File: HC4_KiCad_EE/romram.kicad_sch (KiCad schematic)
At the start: 9 parts, among them J4 AVR-UPDI-6, U1 ATmega4809-A, U2 CH340E

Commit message: 配線進捗、7474を使った変な回路
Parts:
- removed CP11, CP12, CP13: 0.1u, Capacitor_SMD:C_0603_1608Metric, symbol Device2:C_Bypass
- added C2, C3, C4: 0.1u, Capacitor_SMD:C_0603_1608Metric, symbol Device:C
- renumbered C2 to C5
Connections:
- net GND: now also C2.2, C3.2, C4.2
- net VCC: now also C2.1, C3.1, C4.1
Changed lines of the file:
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@@
 		(on_board yes)
 		(dnp no)
-		(property "Reference" "C2"
+		(property "Reference" "C5"
 			(at 163.83 64.7699 0)
 			(effects
@@
 			(project ""
 				(path "/33731ded-38c0-4297-bdd8-92b082f46ff8/ee79785c-5138-4152-a60d-370cd803a828"
-					(reference "C2")
+					(reference "C5")
+					(unit 1)
+				)
+			)
+		)
+	)
+	(symbol
+		(lib_id "Device:C")
+		(at 132.08 163.83 0)
+		(mirror y)
+		(unit 1)
+		(exclude_from_sim no)
+		(in_bom yes)
+		(on_board yes)
+		(dnp no)
+		(property "Reference" "C4"
+			(at 128.27 162.5599 0)
+			(effects
+				(font
+					(size 1.27 1.27)
+				)
+				(justify left)
+			)
+		)
+		(property "Value" "0.1u"
+			(at 128.27 165.0999 0)
+			(effects
+				(font
+					(size 1.27 1.27)
+				)
+				(justify left)
+			)
+		)
+		(property "Footprint" "Capacitor_SMD:C_0603_1608Metric"
+			(at 131.1148 167.64 0)
+			(effects
+				(font
+					(size 1.27 1.27)
+				)
+				(hide yes)
+			)
+		)
+		(property "Datasheet" "~"
+			(at 132.08 163.83 0)
+			(effects
+				(font
+					(size 1.27 1.27)
+				)
+				(hide yes)
+			)
+		)
+		(property "Description" "Unpolarized capacitor"
+			(at 132.08 163.83 0)
+			(effects
+				(font
+					(size 1.27 1.27)
+				)
+				(hide yes)
+			)
+		)
+		(pin "2"
+		)
+		(pin "1"
+		)
+		(instances
+			(project "HC4_KiCad_EE"
+				(path "/33731ded-38c0-4297-bdd8-92b082f46ff8/ee79785c-5138-4152-a60d-370cd803a828"
+					(reference "C4")
 					(unit 1)
 				)
@@
 	)
 	(symbol
-		(lib_id "Device2:C_Bypass")
-		(at 106.68 163.83 0)
-		(unit 1)
-		(exclude_from_sim no)
-		(in_bom yes)
-		(on_board yes)
-		(dnp no)
-		(fields_autoplaced yes)
-		(property "Reference" "CP11"
-			(at 110.49 162.5599 0)
-			(effects
-				(font
-					(size 1.27 1.27)
-				)
-				(justify left)
-			)
-		)
-		(property "Value" "0.1u"
-			(at 110.49 165.0999 0)
-			(effects
-				(font
-					(size 1.27 1.27)
-				)
-				(justify left)
-			)
-		)
-		(property "Footprint" "Capacitor_SMD:C_0603_1608Metric"
-			(at 107.6452 167.64 0)
-			(effects
-				(font
-					(size 1.27 1.27)
-				)
-				(hide yes)
-			)
-		)
-		(property "Datasheet" "~"
-			(at 106.68 163.83 0)
-			(effects
-				(font
-					(size 1.27 1.27)
-				)
-				(hide yes)
-			)
-		)
-		(property "Description" "Bypass Capacitor"
-			(at 106.68 163.83 0)
-			(effects
-				(font
-					(size 1.27 1.27)
-				)
-				(hide yes)
-			)
-		)
-		(pin "1"
-		)
-		(pin "2"
-		)
-		(instances
-			(project ""
-				(path "/33731ded-38c0-4297-bdd8-92b082f46ff8/ee79785c-5138-4152-a60d-370cd803a828"
-					(reference "CP11")
-					(unit 1)
-				)
-			)
-		)
-	)
-	(symbol
 		(lib_id "Device2:LED_")
 		(at 147.32 105.41 90)
@@
 	)
 	(symbol
+		(lib_id "Device:C")
+		(at 106.68 163.83 0)
+		(mirror y)
+		(unit 1)
+		(exclude_from_sim no)
+		(in_bom yes)
+		(on_board yes)
+		(dnp no)
+		(property "Reference" "C2"
+			(at 102.87 162.5599 0)
+			(effects
+				(font
+					(size 1.27 1.27)
+				)
+				(justify left)
+			)
+		)
+		(property "Value" "0.1u"
+			(at 102.87 165.0999 0)
+			(effects
+				(font
+					(size 1.27 1.27)
+				)
+				(justify left)
+			)
+		)
+		(property "Footprint" "Capacitor_SMD:C_0603_1608Metric"
+			(at 105.7148 167.64 0)
+			(effects
+				(font
+					(size 1.27 1.27)
+				)
+				(hide yes)
+			)
+		)
+		(property "Datasheet" "~"
+			(at 106.68 163.83 0)
+			(effects
+				(font
+					(size 1.27 1.27)
+				)
+				(hide yes)
+			)
+		)
+		(property "Description" "Unpolarized capacitor"
+			(at 106.68 163.83 0)
+			(effects
+				(font
+					(size 1.27 1.27)
+				)
+				(hide yes)
+			)
+		)
+		(pin "2"
+		)
+		(pin "1"
+		)
+		(instances
+			(project "HC4_KiCad_EE"
+				(path "/33731ded-38c0-4297-bdd8-92b082f46ff8/ee79785c-5138-4152-a60d-370cd803a828"
+					(reference "C2")
+					(unit 1)
+				)
+			)
+		)
+	)
+	(symbol
 		(lib_id "power:VCC")
 		(at 54.61 57.15 0)
@@
 	)
 	(symbol
-		(lib_id "Device2:C_Bypass")
-		(at 119.38 163.83 0)
-		(unit 1)
-		(exclude_from_sim no)
-		(in_bom yes)
-		(on_board yes)
-		(dnp no)
-		(fields_autoplaced yes)
-		(property "Reference" "CP12"
-			(at 123.19 162.5599 0)
-			(effects
-				(font
-					(size 1.27 1.27)
-				)
-				(justify left)
-			)
-		)
-		(property "Value" "0.1u"
-			(at 123.19 165.0999 0)
-			(effects
-				(font
-					(size 1.27 1.27)
-				)
-				(justify left)
-			)
-		)
-		(property "Footprint" "Capacitor_SMD:C_0603_1608Metric"
-			(at 120.3452 167.64 0)
-			(effects
-				(font
-					(size 1.27 1.27)
-				)
-				(hide yes)
-			)
-		)
-		(property "Datasheet" "~"
-			(at 119.38 163.83 0)
-			(effects
-				(font
-					(size 1.27 1.27)
-				)
-				(hide yes)
-			)
-		)
-		(property "Description" "Bypass Capacitor"
-			(at 119.38 163.83 0)
-			(effects
-				(font
-					(size 1.27 1.27)
-				)
-				(hide yes)
-			)
-		)
-		(pin "1"
-		)
-		(pin "2"
-		)
-		(instances
-			(project "HC4_KiCad_EE"
-				(path "/33731ded-38c0-4297-bdd8-92b082f46ff8/ee79785c-5138-4152-a60d-370cd803a828"
-					(reference "CP12")
-					(unit 1)
-				)
-			)
-		)
-	)
-	(symbol
 		(lib_id "power:VCC")
 		(at 85.09 69.85 0)
@@
 	)
 	(symbol
+		(lib_id "Device:C")
+		(at 119.38 163.83 0)
+		(mirror y)
+		(unit 1)
+		(exclude_from_sim no)
+		(in_bom yes)
+		(on_board yes)
+		(dnp no)
+		(property "Reference" "C3"
+			(at 115.57 162.5599 0)
+			(effects
+				(font
+					(size 1.27 1.27)
+				)
+				(justify left)
+			)
+		)
+		(property "Value" "0.1u"
+			(at 115.57 165.0999 0)
+			(effects
+				(font
+					(size 1.27 1.27)
+				)
+				(justify left)
+			)
+		)
+		(property "Footprint" "Capacitor_SMD:C_0603_1608Metric"
+			(at 118.4148 167.64 0)
+			(effects
+				(font
+					(size 1.27 1.27)
+				)
+				(hide yes)
+			)
+		)
+		(property "Datasheet" "~"
+			(at 119.38 163.83 0)
+			(effects
+				(font
+					(size 1.27 1.27)
+				)
+				(hide yes)
+			)
+		)
+		(property "Description" "Unpolarized capacitor"
+			(at 119.38 163.83 0)
+			(effects
+				(font
+					(size 1.27 1.27)
+				)
+				(hide yes)
+			)
+		)
+		(pin "2"
+		)
+		(pin "1"
+		)
+		(instances
+			(project "HC4_KiCad_EE"
+				(path "/33731ded-38c0-4297-bdd8-92b082f46ff8/ee79785c-5138-4152-a60d-370cd803a828"
+					(reference "C3")
+					(unit 1)
+				)
+			)
+		)
+	)
+	(symbol
 		(lib_id "power:GND")
 		(at 156.21 62.23 0)
@@
 					(unit 1)
 				)
-			)
-		)
-	)
-	(symbol
-		(lib_id "Device2:C_Bypass")
-		(at 132.08 163.83 0)
-		(unit 1)
-		(exclude_from_sim no)
-		(in_bom yes)
-		(on_board yes)
-		(dnp no)
-		(fields_autoplaced yes)
-		(property "Reference" "CP13"
-			(at 135.89 162.5599 0)
-			(effects
-				(font
-					(size 1.27 1.27)
-				)
-				(justify left)
-			)
-		)
-		(property "Value" "0.1u"
-			(at 135.89 165.0999 0)
-			(effects
-				(font
-					(size 1.27 1.27)
-				)
-				(justify left)
-			)
-		)
-		(property "Footprint" "Capacitor_SMD:C_0603_1608Metric"
-			(at 133.0452 167.64 0)
-			(effects
-				(font
-					(size 1.27 1.27)
-				)
-				(hide yes)
-			)
-		)
-		(property "Datasheet" "~"
-			(at 132.08 163.83 0)
-			(effects
-				(font
-					(size 1.27 1.27)
-				)
-				(hide yes)
-			)
-		)
-		(property "Description" "Bypass Capacitor"
-			(at 132.08 163.83 0)
-			(effects
-				(font
-					(size 1.27 1.27)
-				)
-				(hide yes)
-			)
-		)
-		(pin "1"
-		)
-		(pin "2"
-		)
-		(instances
-			(project "HC4_KiCad_EE"
-				(path "/33731ded-38c0-4297-bdd8-92b082f46ff8/ee79785c-5138-4152-a60d-370cd803a828"
-					(reference "CP13")
-					(unit 1)
-				)

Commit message: たぶん完成！！！！！！！
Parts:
- LD31: value ACT -> Chip
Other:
- title: HC4_CPU -> HC4e_CPU
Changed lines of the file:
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@@
 	(paper "A4")
 	(title_block
-		(title "HC4_CPU")
-		(date "2025-06-16")
+		(title "HC4e_CPU")
+		(date "2025-07-21")
 		(rev "1.0")
 	)
@@
 			)
 		)
-		(property "Value" "ACT"
+		(property "Value" "Chip"
 			(at 151.13 108.2675 90)
 			(effects

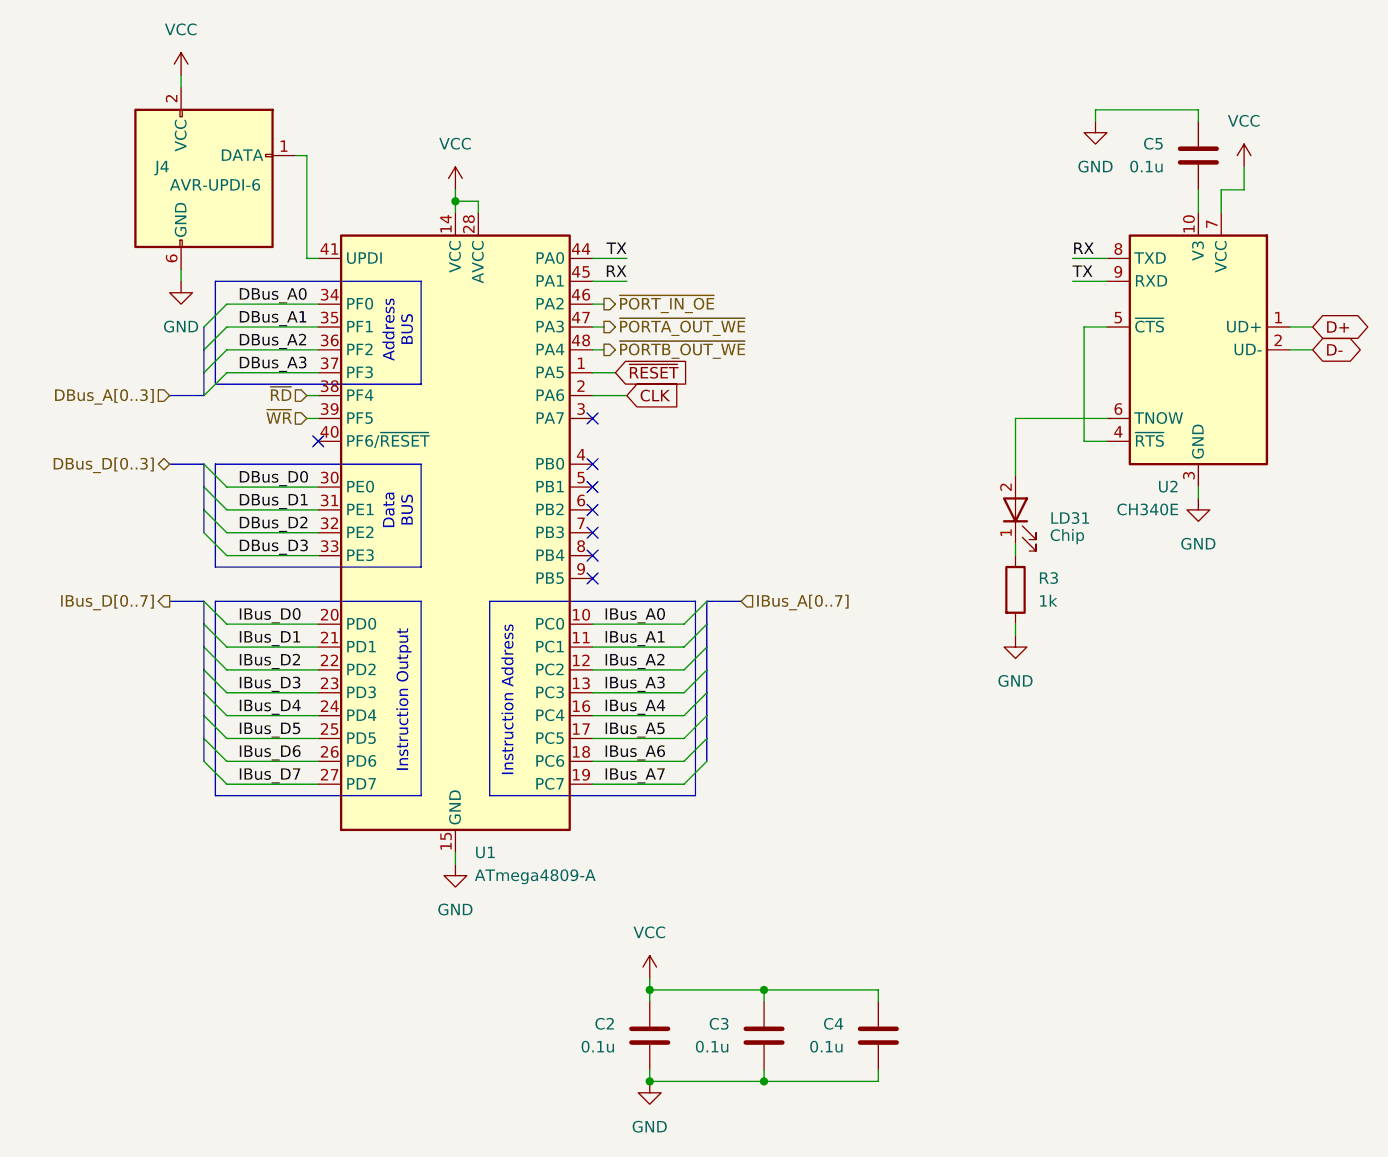
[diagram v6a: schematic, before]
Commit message: HC4e設計変更:CH340に敗北宣言、USBシリアル仕様に変更
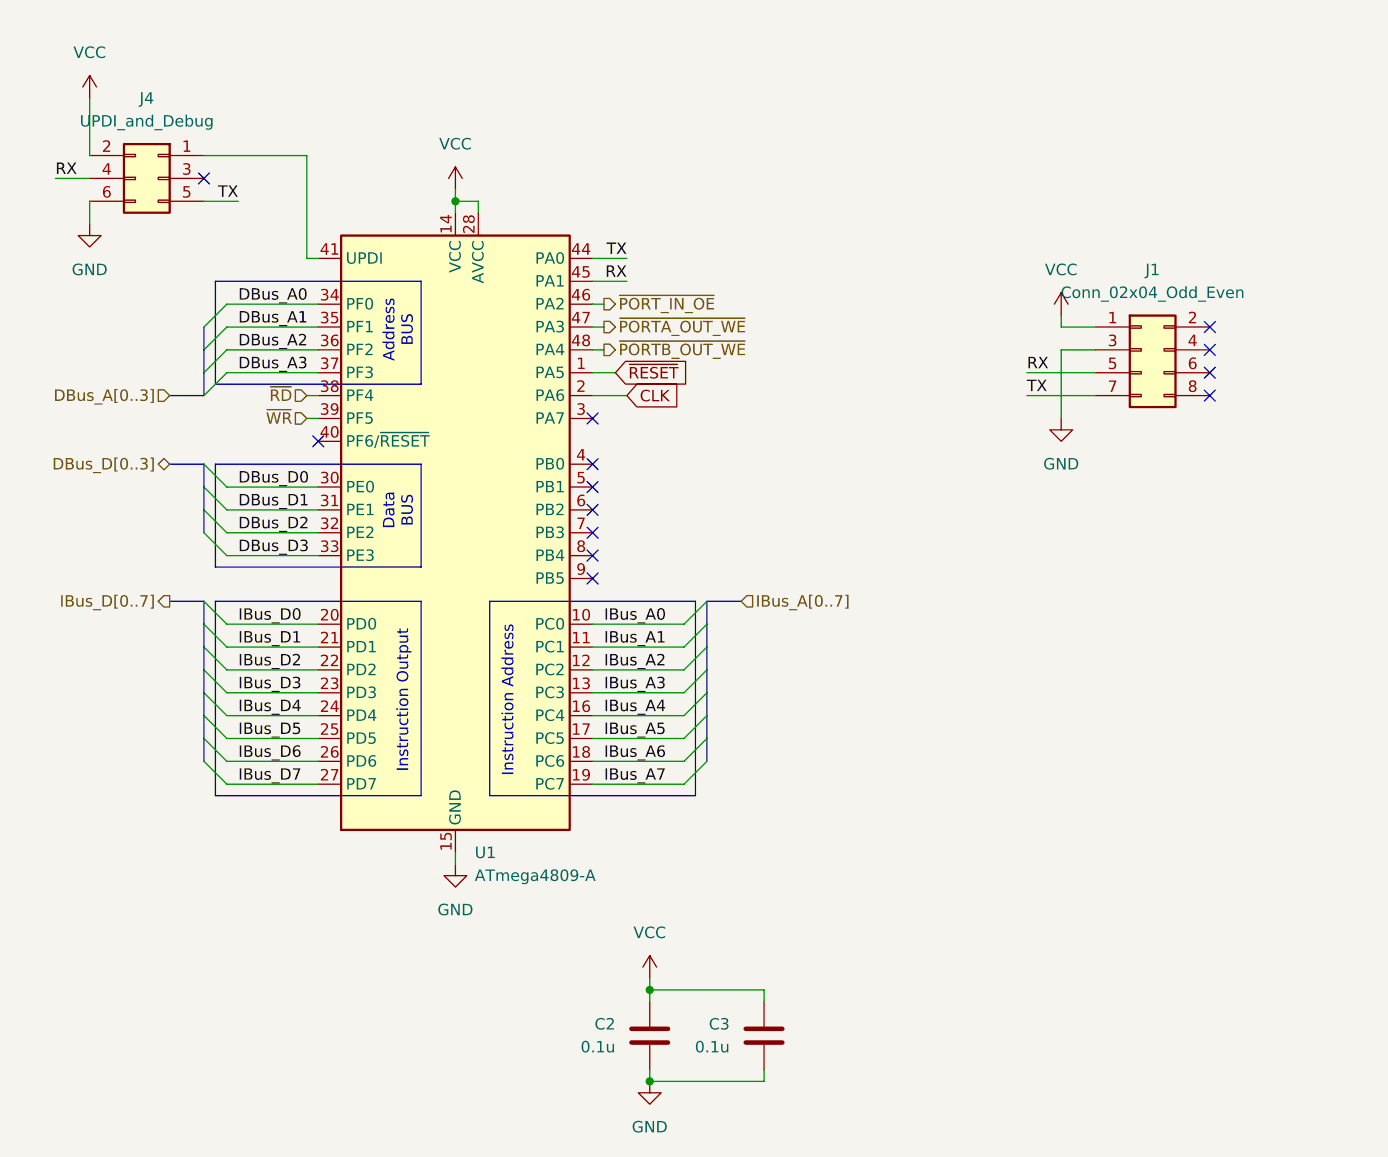
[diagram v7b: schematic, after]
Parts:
- removed C4, C5: 0.1u, Capacitor_SMD:C_0603_1608Metric, symbol Device:C
- removed J4: AVR-UPDI-6, Connector_PinHeader_2.54mm:PinHeader_2x03_P2.54mm_Vertical, symbol Connector:AVR-UPDI-6
- removed LD31: Chip, LED_SMD:LED_0603_1608Metric, symbol Device2:LED_
- removed R3: 1k, Resistor_SMD:R_0603_1608Metric, symbol Device:R
- removed U2: CH340E, Package_SO:MSOP-10_3x3mm_P0.5mm, symbol Interface_USB:CH340E
- added J1: Conn_02x04_Odd_Even, Connector_PinHeader_2.54mm:PinHeader_2x04_P2.54mm_Vertical, symbol Connector_Generic:Conn_02x04_Odd_Even
- added J4: UPDI_and_Debug, Connector_PinHeader_2.54mm:PinHeader_2x03_P2.54mm_Vertical, symbol Connector_Generic:Conn_02x03_Odd_Even
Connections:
- net GND: now also J1.3 (Pin_3), J4.6 (Pin_6)
- net RX: now also J1.5 (Pin_5), J4.4 (Pin_4)
- net TX: now also J1.7 (Pin_7), J4.5 (Pin_5)
- net VCC: now also J1.1 (Pin_1), J4.2 (Pin_2)
- net at U1.41 (UPDI): now also J4.1 (Pin_1)
- no-connect marks 8 -> 13
